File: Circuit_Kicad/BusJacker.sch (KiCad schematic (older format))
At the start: 18 parts

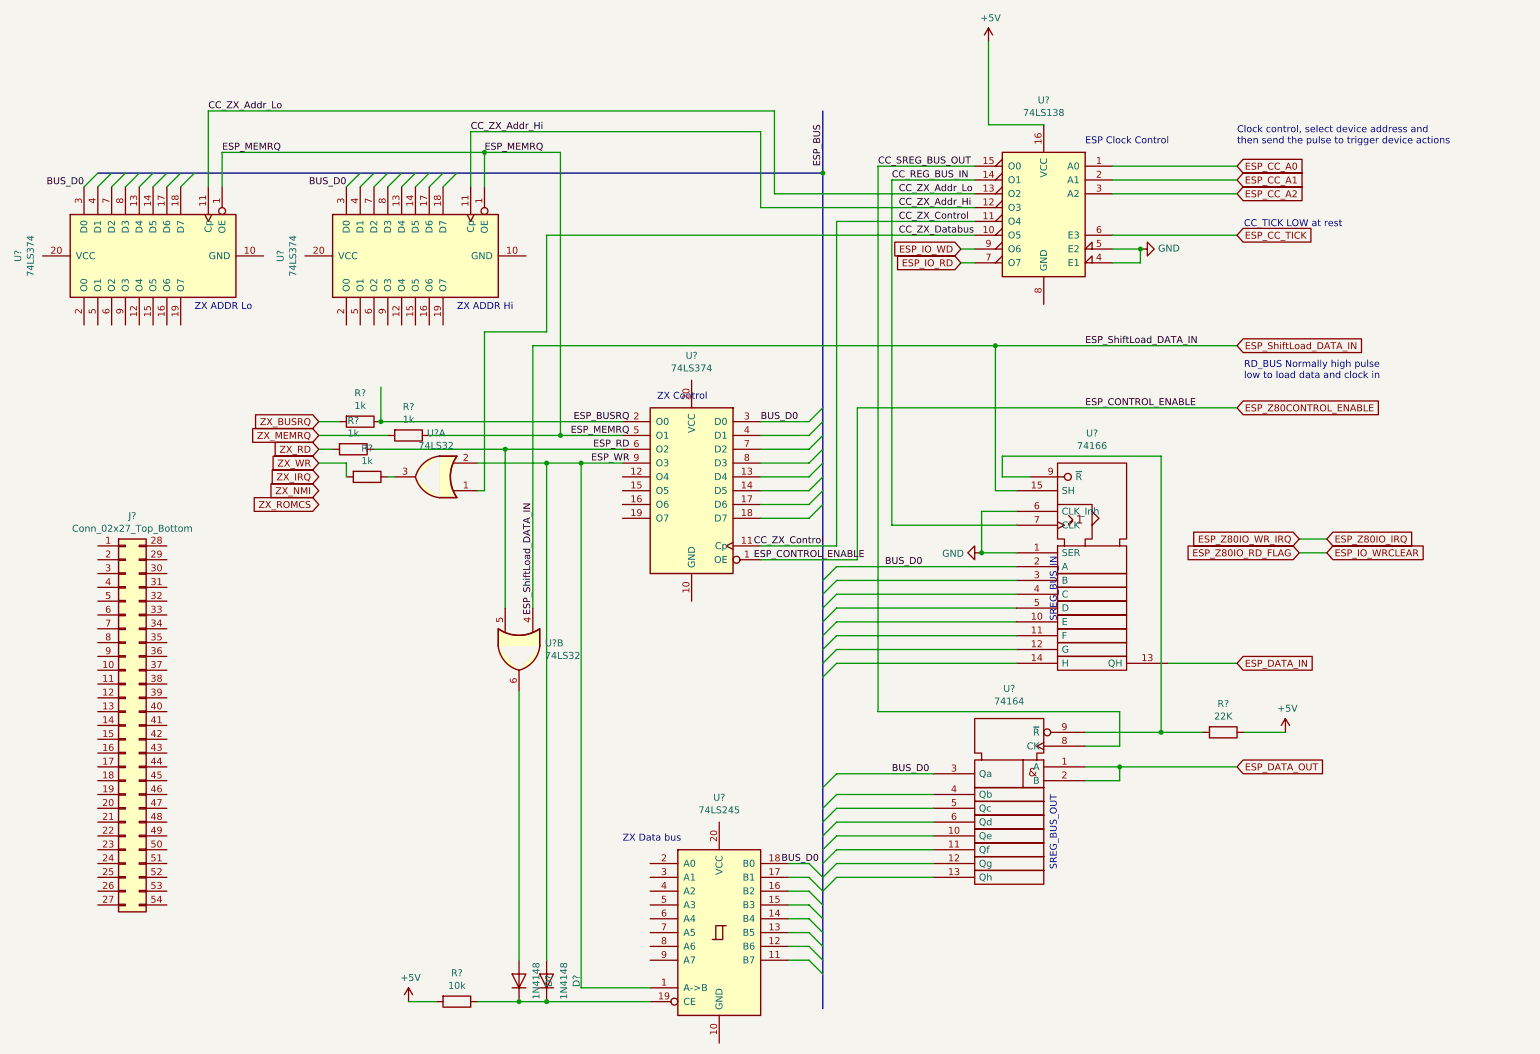
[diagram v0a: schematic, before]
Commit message: Aligning Circuit and Code names
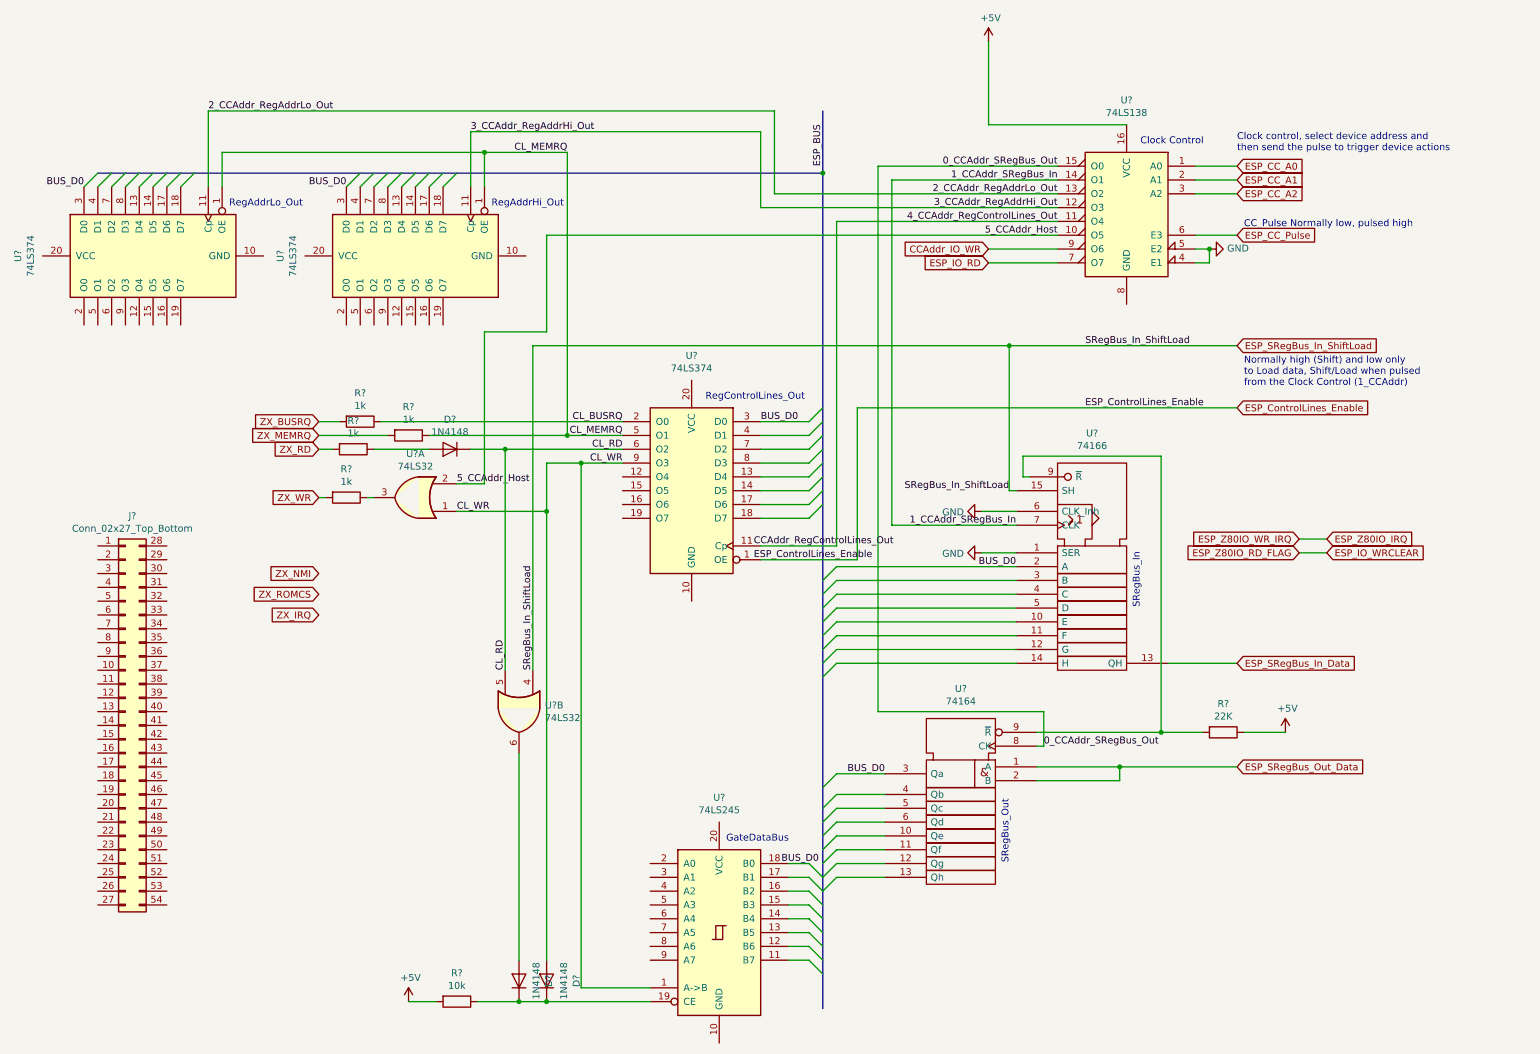
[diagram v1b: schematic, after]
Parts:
- added D?: 1N4148, Diode_THT:D_DO-35_SOD27_P7.62mm_Horizontal, symbol Diode:1N4148
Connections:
- net CL_WR: now reaches D?.2 (A), U?.1 (A->B), U?.9 (O3)
- net CL_WR: now also U?.1; no longer U?.2
- net CL_BUSRQ: now reaches R?.1, U?.2 (O0)
- net CL_RD: now reaches U?.5, U?.6 (O2)
- net CL_RD: now also D?.1 (K); no longer R?.1
- net CC_REG_BUS_IN renamed 1_CCAddr_SRegBus_In
- net CC_SREG_BUS_OUT renamed 0_CCAddr_SRegBus_Out
- net CC_ZX_Addr_Hi renamed 3_CCAddr_RegAddrHi_Out
- net CC_ZX_Addr_Lo renamed 2_CCAddr_RegAddrLo_Out
- net CC_ZX_Control renamed 4_CCAddr_RegControlLines_Out
- net CC_ZX_Databus renamed 5_CCAddr_Host
- net 5_CCAddr_Host: now also U?.2; no longer U?.1
- net ESP_CC_TICK renamed ESP_CC_Pulse
- net ESP_DATA_IN renamed ESP_SRegBus_In_Data
- net ESP_DATA_OUT renamed ESP_SRegBus_Out_Data
- net ESP_IO_WD renamed CCAddr_IO_WR
- net ESP_MEMRQ renamed CL_MEMRQ
- net ESP_ShiftLoad_DATA_IN renamed ESP_SRegBus_In_ShiftLoad
- net ESP_Z80CONTROL_ENABLE renamed ESP_ControlLines_Enable
- new net: D?.2 (A), R?.1
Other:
- note added: "CC_Pulse Normally low, pulsed high\n"
- note added: "Clock Control"
- note added: "GateDataBus"
- note added: "Normally high (Shift) and low only \nto Load data, Shift/Load when pulsed \nfrom the Clock Control (1_CCAddr)"
- note added: "RegAddrHi_Out"
- note added: "RegAddrLo_Out"
- note added: "RegControlLines_Out"
- note added: "SRegBus_In"
- note added: "SRegBus_Out\n"
- note removed: "CC_TICK LOW at rest\n"
- note removed: "ESP Clock Control"
- note removed: "RD_BUS Normally high pulse\nlow to load data and clock in"
- note removed: "SREG_BUS_IN"
- note removed: "SREG_BUS_OUT"
- note removed: "ZX ADDR Hi"
- note removed: "ZX ADDR Lo"
- note removed: "ZX Control"
- note removed: "ZX Data bus"
- moved on the sheet: R?, U?, U?A, U?B
